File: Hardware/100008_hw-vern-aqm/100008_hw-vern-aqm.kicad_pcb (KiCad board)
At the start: 6 copper layers, 0 parts

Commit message: schematic and pcb work
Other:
- board outline added: 98 x 56.3 mm

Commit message: schematic and pcb layout
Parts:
- added C1: 1u, Capacitor_SMD:C_0805_2012Metric, F.Cu at (184.0, 324.5)
- added C10: 10u, Capacitor_SMD:C_0805_2012Metric, F.Cu at (108.9, 301.9)
- added C11: 10u, Capacitor_SMD:C_0805_2012Metric, F.Cu at (108.9, 303.9)
- added C12: 100n, Capacitor_SMD:C_0603_1608Metric, F.Cu at (221.2, 407.9)
- added C13: 100n, Capacitor_SMD:C_0603_1608Metric, F.Cu at (165.5, 313.0)
- added C14: 10u, Capacitor_SMD:C_0805_2012Metric, F.Cu at (162.1, 319.4)
- added C15: 100n, Capacitor_SMD:C_0603_1608Metric, F.Cu at (165.5, 316.2)
- added C16: 100n, Capacitor_SMD:C_0603_1608Metric, F.Cu at (146.4, 339.7)
- added C17: 100n, Capacitor_SMD:C_0603_1608Metric, F.Cu at (125.9, 351.8)
- added C18: 100n, Capacitor_SMD:C_0603_1608Metric, F.Cu at (144.8, 339.7)
- added C19: 100n, Capacitor_SMD:C_0603_1608Metric, F.Cu at (111.6, 351.8)
- added C2: 10u, Capacitor_SMD:C_0805_2012Metric, F.Cu at (179.6, 310.8)
- added C3: 10u, Capacitor_SMD:C_0805_2012Metric, F.Cu at (183.1, 310.8)
- added C4: 100n, Capacitor_SMD:C_0603_1608Metric, F.Cu at (179.4, 308.7)
- added C5: 10u, Capacitor_SMD:C_0805_2012Metric, F.Cu at (177.9, 304.2)
- added C6: 10u, Capacitor_SMD:C_0805_2012Metric, F.Cu at (180.0, 304.2)
- added C7: 100n, Capacitor_SMD:C_0603_1608Metric, F.Cu at (351.9, 406.0)
- added C8: 100n, Capacitor_SMD:C_0603_1608Metric, F.Cu at (109.1, 307.2)
- added C9: 100n, Capacitor_SMD:C_0603_1608Metric, F.Cu at (351.9, 411.0)
- added D1: ESD5Z3V3, Diode_SMD:D_SOD-523, F.Cu at (182.2, 334.4)
- added D2: ESD321DYAR, Diode_SMD:D_SOD-523, F.Cu at (182.2, 336.8)
- added D3: ESD321DYAR, Diode_SMD:D_SOD-523, F.Cu at (182.2, 339.3)
- added D4: ESD321DYAR, Diode_SMD:D_SOD-523, F.Cu at (140.1, 306.4)
- added D5: ESD321DYAR, Diode_SMD:D_SOD-523, F.Cu at (143.1, 306.4)
- added D6: LED, LED_SMD:LED_0603_1608Metric, F.Cu at (180.8, 315.1)
- added D7: LED, LED_SMD:LED_0603_1608Metric, F.Cu at (184.5, 315.1)
- added D8: LED, LED_SMD:LED_0603_1608Metric, F.Cu at (158.8, 305.7)
- added D9: LED, LED_SMD:LED_0603_1608Metric, F.Cu at (161.8, 305.7)
- added F1: Polyfuse, Fuse:Fuse_1206_3216Metric, F.Cu at (184.0, 322.3)
- added J1: Conn_01x14_Socket, Connector_PinHeader_2.54mm:PinHeader_1x14_P2.54mm_Vertical, F.Cu at (102.0, 344.7)
- added J2: USB4220-03-1000-C, Mechanical:USB_C_Receptacle_GCT_USB4220-03-xxxx-C_Vertical, F.Cu at (191.0, 328.2)
- added J3: Conn_01x06_MountingPin, Connector_JST:JST_GH_BM06B-GHS-TBT_1x06-1MP_P1.25mm_Vertical, F.Cu at (229.8, 337.8)
- added J4: Conn_01x03_Pin, Connector_PinHeader_2.54mm:PinHeader_1x03_P2.54mm_Vertical, F.Cu at (140.3, 303.1)
- added J5: Conn_01x06_Socket, Connector_PinHeader_2.00mm:PinHeader_1x06_P2.00mm_Vertical, F.Cu at (223.1, 343.0)
- added J6: Conn_01x04_Socket, Connector_PinHeader_2.54mm:PinHeader_1x04_P2.54mm_Vertical, F.Cu at (196.0, 332.0)
- added J7: Conn_01x05_Pin, Connector_PinHeader_2.54mm:PinHeader_1x05_P2.54mm_Vertical, F.Cu at (269.2, 284.4)
- added Q1: BC817, Package_TO_SOT_SMD:SOT-23, F.Cu at (150.1, 312.4)
- added Q2: BC817, Package_TO_SOT_SMD:SOT-23, F.Cu at (150.1, 315.9)
- added R1: 0R0, Resistor_SMD:R_0603_1608Metric, F.Cu at (279.9, 277.5)
- added R10: 0R0, Resistor_SMD:R_0603_1608Metric, F.Cu at (235.8, 333.6)
- added R11: 10k, Resistor_SMD:R_0603_1608Metric, F.Cu at (283.9, 287.6)
- added R12: 10k, Resistor_SMD:R_0603_1608Metric, F.Cu at (122.0, 323.2)
- added R13: 10k, Resistor_SMD:R_0603_1608Metric, F.Cu at (123.5, 323.2)
- added R14: 0R0, Resistor_SMD:R_0603_1608Metric, F.Cu at (179.4, 306.9)
- added R15: 10k, Resistor_SMD:R_0603_1608Metric, F.Cu at (182.4, 315.1)
- added R16: 10k, Resistor_SMD:R_0603_1608Metric, F.Cu at (186.1, 315.1)
- added R17: 10k, Resistor_SMD:R_0603_1608Metric, F.Cu at (109.1, 308.7)
- added R18: 5k1, Resistor_SMD:R_0603_1608Metric, F.Cu at (165.5, 309.8)
- added R19: 10k, Resistor_SMD:R_0603_1608Metric, F.Cu at (165.5, 311.4)
- added R2: 0R0, Resistor_SMD:R_0603_1608Metric, F.Cu at (279.9, 280.0)
- added R20: 1k, Resistor_SMD:R_0603_1608Metric, F.Cu at (165.5, 314.6)
- added R21: 0R0, Resistor_SMD:R_0603_1608Metric, F.Cu at (160.7, 323.9)
- added R22: 0R0, Resistor_SMD:R_0603_1608Metric, F.Cu at (159.2, 323.9)
- added R23: 10k, Resistor_SMD:R_0603_1608Metric, F.Cu at (153.7, 316.4)
- added R24: 10k, Resistor_SMD:R_0603_1608Metric, F.Cu at (153.7, 311.8)
- added R25: 0R0, Resistor_SMD:R_0603_1608Metric, F.Cu at (153.7, 314.9)
- added R26: 0R0, Resistor_SMD:R_0603_1608Metric, F.Cu at (153.7, 313.4)
- added R27: 10k, Resistor_SMD:R_0603_1608Metric, F.Cu at (158.8, 308.8)
- added R28: 1k, Resistor_SMD:R_0603_1608Metric, F.Cu at (160.3, 308.8)
- added R29: 1k, Resistor_SMD:R_0603_1608Metric, F.Cu at (161.8, 308.8)
- added R3: 5k1, Resistor_SMD:R_0603_1608Metric, F.Cu at (184.7, 328.9)
- added R30: 0R0, Resistor_SMD:R_0603_1608Metric, F.Cu at (153.7, 310.3)
- added R31: 0R0, Resistor_SMD:R_0603_1608Metric, F.Cu at (153.7, 317.9)
- added R32: 10k, Resistor_SMD:R_0603_1608Metric, F.Cu at (134.6, 302.7)
- added R33: 10k, Resistor_SMD:R_0603_1608Metric, F.Cu at (134.6, 304.2)
- added R34: 10k, Resistor_SMD:R_0603_1608Metric, F.Cu at (143.2, 339.7)
- added R4: 5k1, Resistor_SMD:R_0603_1608Metric, F.Cu at (184.7, 327.4)
- added R5: 0R0, Resistor_SMD:R_0603_1608Metric, F.Cu at (177.4, 327.6)
- added R6: 0R0, Resistor_SMD:R_0603_1608Metric, F.Cu at (177.3, 325.8)
- added R7: 0R0, Resistor_SMD:R_0603_1608Metric, F.Cu at (236.0, 339.4)
- added R8: 100R, Resistor_SMD:R_0603_1608Metric, F.Cu at (141.6, 306.4)
- added R9: 100R, Resistor_SMD:R_0603_1608Metric, F.Cu at (144.6, 306.4)
- added SW1: SW_Push, Button_Switch_SMD:SW_Tactile_SPST_NO_Straight_CK_PTS636Sx25SMTRLFS, F.Cu at (343.6, 406.0)
- added SW2: SW_Push, Button_Switch_SMD:SW_Tactile_SPST_NO_Straight_CK_PTS636Sx25SMTRLFS, F.Cu at (343.6, 411.2)
- added TP1: TestPoint, TestPoint:TestPoint_Pad_D1.5mm, F.Cu at (297.4, 298.9)
- added TP2: TestPoint, TestPoint:TestPoint_Pad_D1.5mm, F.Cu at (297.4, 302.5)
- added U1: AMS1117-3.3, Package_TO_SOT_SMD:SOT-223-3_TabPin2, F.Cu at (185.6, 306.1)
- added U2: ESP32-S3-WROOM-1, PCM_Espressif:ESP32-S3-WROOM-1, F.Cu at (121.8, 309.8)
- added U3: CP2102N-Axx-xQFN24, Package_DFN_QFN:QFN-24-1EP_4x4mm_P0.5mm_EP2.6x2.6mm, F.Cu at (159.9, 314.4)
- added U4: SCD40-D-R2, Sensor:Sensirion_SCD4x-1EP_10.1x10.1mm_P1.25mm_EP4.8x4.8mm, F.Cu at (118.8, 349.8)
- added U5: DPS368, Components:LGA8S145X65P2X4_200X250X110-V, F.Cu at (145.3, 346.1)
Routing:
- net +3V3: track 0.00 -> 9.73 mm
- net GND: track 0.00 -> 8.05 mm, vias 0 -> 1
- net Net-(U5-SDO): track 0.00 -> 5.28 mm
- net unconnected-(U5-~{CSB}-Pad2): track 0.00 -> 4.05 mm
- net I2C_SDA: track 0.00 -> 4.05 mm
- net I2C_SCL: track 0.00 -> 4.05 mm

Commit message: schematic and pcb general layout
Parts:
- added H2: MountingHole, MountingHole:MountingHole_4.5mm, F.Cu at (195.0, 352.9)
- added H3: MountingHole, MountingHole:MountingHole_4.5mm, F.Cu at (195.0, 303.4)
- added H4: MountingHole, MountingHole:MountingHole_4.5mm, F.Cu at (103.0, 303.4)
- moved C9 249.0 mm to (118.6, 324.0)
- moved SW2 240.0 mm to (117.8, 329.7), turned to -90 degrees
- moved C7 239.3 mm to (127.2, 324.0), turned to 180 degrees
- moved SW1 228.8 mm to (127.8, 329.7), turned to -90 degrees
- moved R1 184.6 mm to (109.0, 347.3)
- moved R2 182.8 mm to (109.0, 344.7)
- moved R11 166.5 mm to (121.3, 323.2), turned to 90 degrees
- moved C12 150.9 mm to (110.2, 305.7), turned to 180 degrees
- moved J7 135.2 mm to (140.4, 325.5), turned to 180 degrees
- moved TP2 88.5 mm to (209.9, 315.8)
- moved TP1 85.3 mm to (213.8, 315.7)
- moved R10 62.8 mm to (173.2, 339.3)
- moved R7 60.9 mm to (175.5, 346.2), turned to 180 degrees
- moved J3 53.2 mm to (178.2, 350.6), turned to 180 degrees
- moved J5 39.9 mm to (183.2, 343.3), turned to -90 degrees
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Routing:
- net JTAG_TCK: track 0.00 -> 17.9 mm
- net JTAG_TDO: track 0.00 -> 16.4 mm
- net UART0_RX: track 0.00 -> 16.2 mm
- net JTAG_TDI: track 0.00 -> 15.4 mm
- net JTAG_TMS: track 0.00 -> 14.1 mm
- net UART0_TX: track 0.00 -> 12.4 mm
- net Net-(D1-K): track 0.00 -> 5.84 mm
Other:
- outline, holes or cut-outs redrawn
- board text added: "3V3"
- board text added: "BACKLIGHT"
- board text added: "CS"
- board text added: "DC/RS"
- board text added: "GND"
- board text added: "GPIO0"
- board text added: "MISO"
- board text added: "MOSI"
- board text added: "RESET"
- board text added: "RX"
- board text added: "SCK"
- board text added: "SCL"
- board text added: "SDA"
- board text added: "TCK"
- board text added: "TDI"
- board text added: "TDO"
- board text added: "TMS"
- board text added: "TX"
- board text added: "T_CLK"
- board text added: "T_CS"
- board text added: "T_DIN"
- board text added: "T_IRQ"
- board text added: "T_OUT"
- board text added: "VBUS"
- board text added: "VCC"

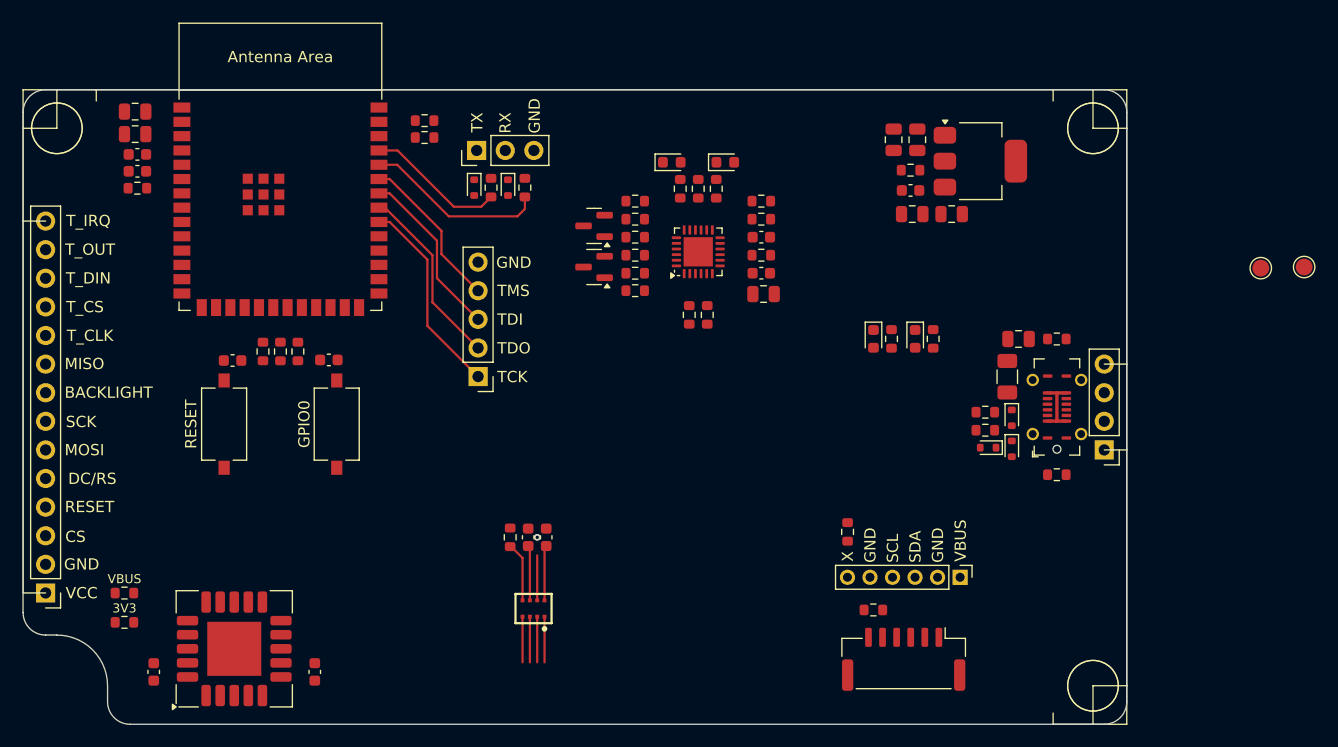
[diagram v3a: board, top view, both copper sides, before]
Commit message: schematic, pcb layout, added mouser shoping cart
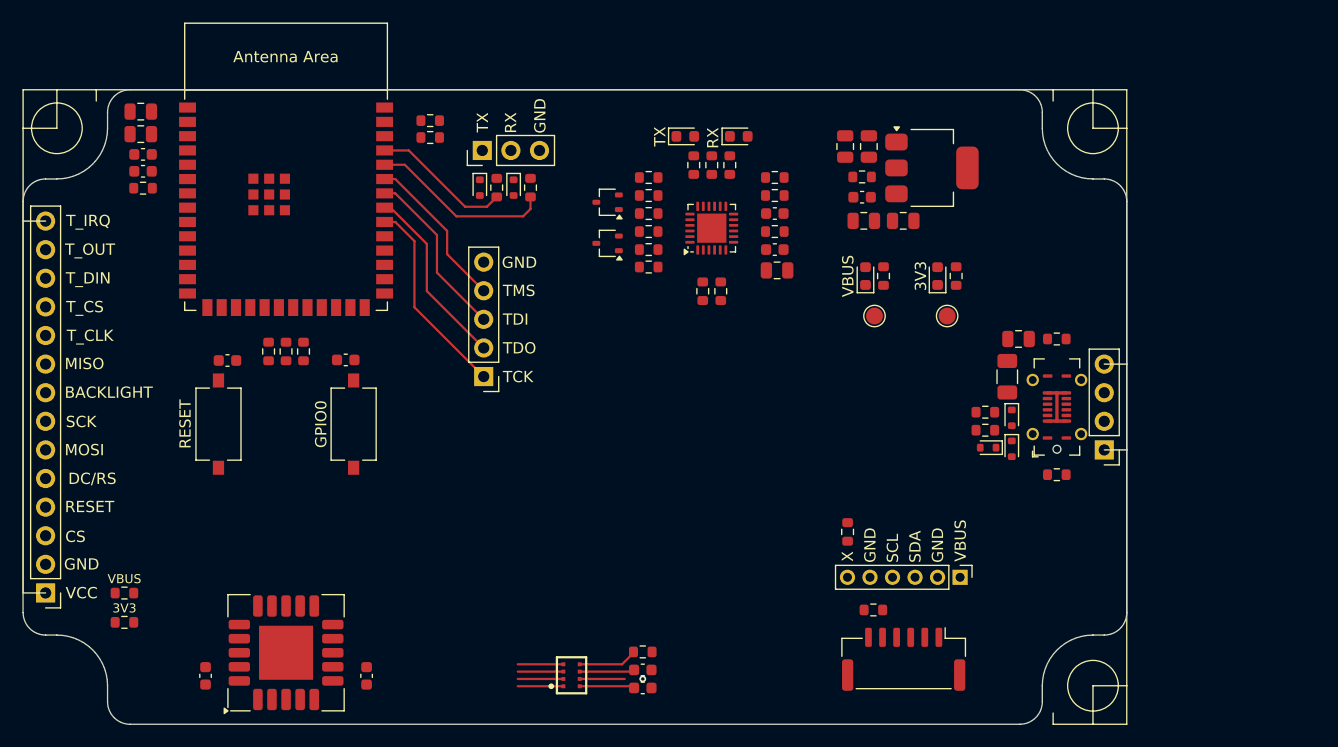
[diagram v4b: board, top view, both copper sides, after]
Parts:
- removed H2, H3, H4: MountingHole, MountingHole:MountingHole_4.5mm
- Q1, Q2: footprint Package_TO_SOT_SMD:SOT-23 -> Package_TO_SOT_SMD:SOT-323_SC-70
- moved TP1 38.4 mm to (175.6, 320.1)
- moved TP2 28.2 mm to (182.1, 320.1)
- moved C16 15.9 mm to (155.0, 353.1), turned to 0 degrees
- moved R34 15.6 mm to (155.0, 349.9), turned to 0 degrees
- moved C18 15.6 mm to (155.0, 351.5), turned to 0 degrees
- moved U5 6.82 mm to (148.7, 352.0), turned to 90 degrees
- moved R16 5.94 mm to (182.8, 316.5)
- moved D7 5.92 mm to (181.2, 316.5), turned to 90 degrees
- moved R15 5.62 mm to (176.4, 316.5)
- moved D6 5.62 mm to (174.8, 316.5), turned to 90 degrees
- moved C19 4.61 mm to (116.2, 352.0)
- moved C17 4.61 mm to (130.5, 352.0)
- moved U4 4.61 mm to (123.3, 350.0)
- moved C4 4.34 mm to (174.5, 309.5)
- moved C5 4.34 mm to (173.0, 305.0)
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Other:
- outline, holes or cut-outs redrawn

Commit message: pcb routing
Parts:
- added J8: Conn_01x04_MountingPin, Connector_JST:JST_SH_SM04B-SRSS-TB_1x04-1MP_P1.00mm_Horizontal, F.Cu at (184.5, 353.3)
- moved R10 14.5 mm to (160.3, 345.8), turned to -90 degrees
- moved R7 13.7 mm to (161.8, 345.8), turned to 90 degrees
- moved J5 9.52 mm to (174.0, 345.8)
- moved J3 9.38 mm to (169.0, 352.5)
- moved C16 3.69 mm to (151.3, 353.4)
- moved C18 3.69 mm to (151.3, 351.8)
- moved R34 3.69 mm to (151.3, 350.2)
- moved U5 3.69 mm to (145.0, 352.3)
- moved J7 1.71 mm to (140.8, 323.8)
- moved R11 1.55 mm to (121.8, 324.8)
- moved R12 1.55 mm to (123.3, 324.8)
- moved R13 1.55 mm to (124.9, 324.8)
- moved C4 0.92 mm to (175.4, 309.3)
- moved C5 0.92 mm to (173.9, 304.8)
- moved C6 0.92 mm to (176.0, 304.8)
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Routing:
- net USB_D-: track 0.00 -> 57.5 mm, vias 0 -> 2
- net USB_D+: track 0.00 -> 55.6 mm, vias 0 -> 2
- net +3V3: track 9.73 -> 50.7 mm
- net Net-(D3-K): track 0.00 -> 12.8 mm, vias 0 -> 2
- net Net-(D1-K): track 5.84 -> 17.2 mm, vias 0 -> 4
- net Net-(U3-VBUS): track 0.00 -> 9.57 mm
- net /Project Architecture/MCU - ESP32/GPIO0: track 0.00 -> 8.86 mm
- net Net-(D2-K): track 0.00 -> 8.18 mm
- net Net-(J2-CC2): track 0.00 -> 7.89 mm
- net Net-(J2-CC1): track 0.00 -> 7.78 mm, vias 0 -> 2
- net SD_CS(D3): track 0.00 -> 5.00 mm
- net SD_MOSI(CMD): track 0.00 -> 4.89 mm
- net SD_MISO(D0): track 0.00 -> 4.77 mm
- net Net-(D5-K): track 0.00 -> 4.27 mm
- net Net-(U3-~{SUSPEND}): track 0.00 -> 4.26 mm
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- added copper zone on F.Cu, net GND
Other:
- copper layers 6 -> 2
- board text added: "Air Quality Meter for VERN' University"
- board text added: "DPS368"
- board text added: "Designed by Šimunčić A."
- board text added: "SCD40"
- board text added: "SEN5x"
- board text added: "V1.0"
- board text added: "easyC"

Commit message: pcb layout
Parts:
- moved C11 1.67 mm to (109.5, 302.6), turned to 90 degrees
- moved C10 1.19 mm to (111.5, 302.6), turned to 90 degrees
- moved R17 0.78 mm to (110.5, 308.0)
- moved C8 0.75 mm to (110.5, 306.5)
- moved C12 0.73 mm to (110.5, 305.0)
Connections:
- U2 pad 10: SD_SCK(CLK) -> SPI_SCK
- U2 pad 11: unconnected-(U2-GPIO18/U1RXD/ADC2_CH7/CLK_OUT3-Pad11) -> LCD_BACKLIGHT
- U2 pad 12: SPI_SCK -> LCD_DC/RS
- U2 pad 18: LCD_DC/RS -> SPI_nCS_LCD
- U2 pad 19: LCD_BACKLIGHT -> SD_CS(D3)
- U2 pad 20: SD_CS(D3) -> SD_MOSI(CMD)
- U2 pad 21: SD_MOSI(CMD) -> SD_MISO(D0)
- U2 pad 22: SD_MISO(D0) -> SD_SCK(CLK)
- U2 pad 4: SPI_nCS_LCD -> unconnected-(U2-GPIO4/TOUCH4/ADC1_CH3-Pad4)
- U2 pad 5: SPI_nCS_TOUCH -> SPI_MISO
- U2 pad 6: SPI_MISO -> SPI_MOSI
- U2 pad 7: SPI_MOSI -> SPI_nCS_TOUCH
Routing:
- net +3V3: track 50.7 -> 235.9 mm, vias 0 -> 1
- net I2C_SCL: track 7.77 -> 40.5 mm, vias 0 -> 1
- net SPI_MOSI: track 0.00 -> 32.5 mm
- net SPI_nCS_LCD: track 0.00 -> 31.5 mm
- net I2C_SDA: track 7.77 -> 34.8 mm, vias 0 -> 1
- net /Project Architecture/MCU - ESP32/RESET: track 1.79 -> 27.7 mm, vias 0 -> 2
- net SPI_SCK: track 0.00 -> 24.9 mm
- net LCD_RESET: track 0.00 -> 24.7 mm
- net LCD_DC/RS: track 0.00 -> 24.4 mm
- net LCD_BACKLIGHT: track 0.00 -> 19.6 mm
- net SPI_nCS_TOUCH: track 0.00 -> 16.8 mm
- net SPI_MISO: track 0.00 -> 15.7 mm
- net GND: track 8.05 -> 18.4 mm, vias 1 -> 15
- net Net-(J1-Pin_1): track 0.00 -> 8.78 mm
- net Net-(J3-Pin_5): track 0.00 -> 7.83 mm
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
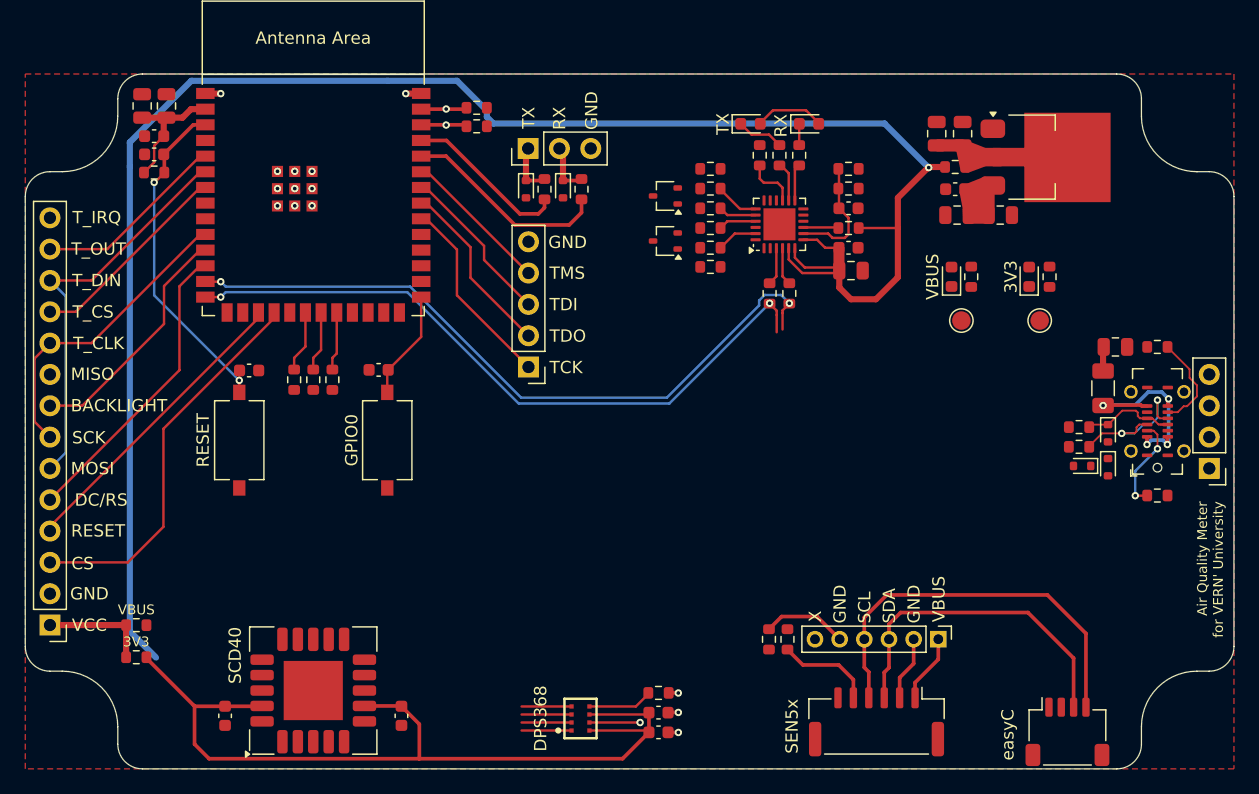
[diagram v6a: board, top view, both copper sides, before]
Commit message: PCB routing and DRC fixes
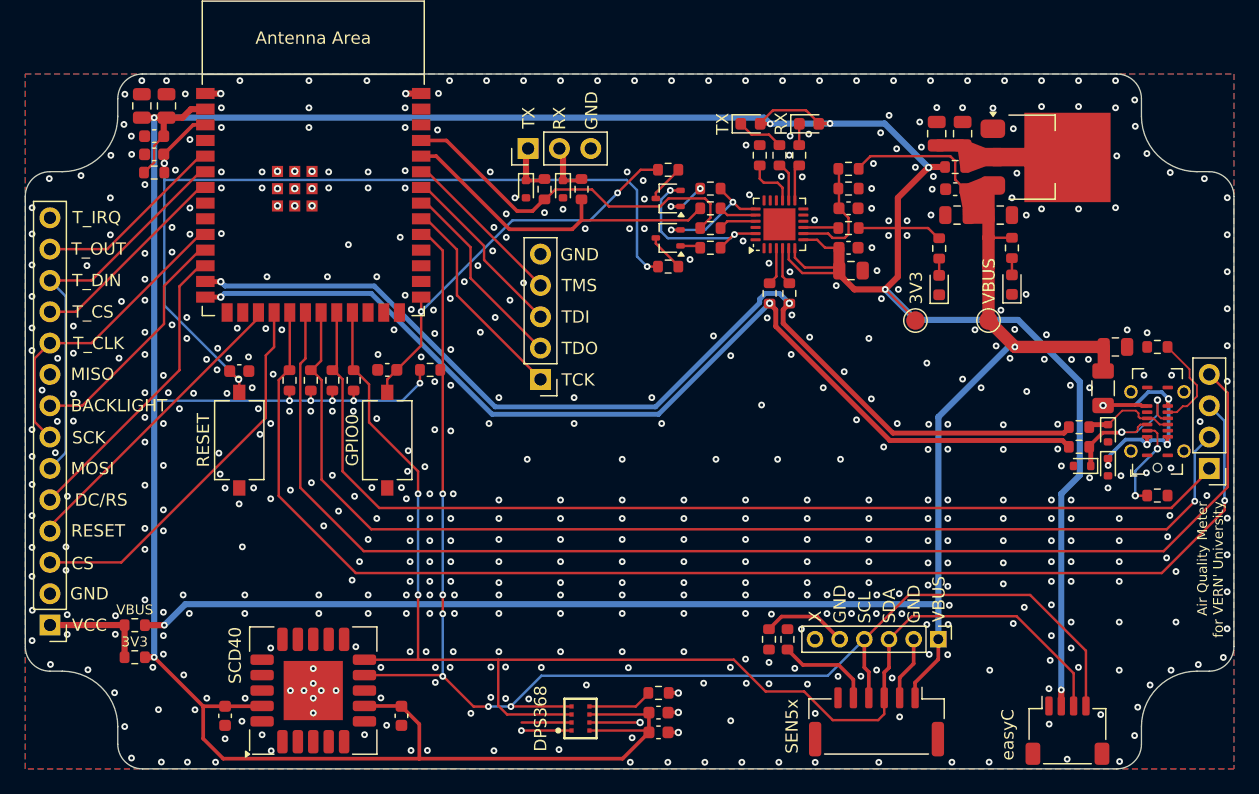
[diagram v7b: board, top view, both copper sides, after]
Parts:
- moved R32 24.2 mm to (126.6, 324.8), turned to 90 degrees
- moved R33 20.1 mm to (132.8, 324.0), turned to 0 degrees
- moved TP2 10.1 mm to (172.2, 320.0)
- moved R16 9.24 mm to (174.1, 314.1)
- moved R30 8.63 mm to (152.1, 315.6), turned to 0 degrees
- moved R31 8.59 mm to (152.1, 307.8), turned to 0 degrees
- moved D7 7.33 mm to (174.1, 317.1)
- moved D6 4.94 mm to (180.0, 317.1)
- moved R15 4.04 mm to (180.0, 314.1)
- moved R13 3.48 mm to (121.4, 324.8)
- moved Q2 3.46 mm to (152.1, 310.1)
- moved Q1 3.41 mm to (152.1, 313.3)
- moved R11 3.10 mm to (124.9, 324.8)
- moved TP1 2.20 mm to (178.1, 320.0)
- moved J7 1.40 mm to (141.8, 324.8)
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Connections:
- U2 pad 19: SD_CS(D3) -> SD_MISO(D0)
- U2 pad 20: SD_MOSI(CMD) -> SD_SCK(CLK)
- U2 pad 21: SD_MISO(D0) -> SD_MOSI(CMD)
- U2 pad 22: SD_SCK(CLK) -> SD_CS(D3)
- U2 pad 23: unconnected-(U2-GPIO21-Pad23) -> I2C_SDA
- U2 pad 31: unconnected-(U2-GPIO38/FSPIWP/SUBSPIWP-Pad31) -> I2C_SCL
- U2 pad 38: I2C_SCL -> unconnected-(U2-GPIO2/TOUCH2/ADC1_CH1-Pad38)
- U2 pad 39: I2C_SDA -> unconnected-(U2-GPIO1/TOUCH1/ADC1_CH0-Pad39)
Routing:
- net VBUS: track 7.50 -> 131.0 mm, vias 0 -> 2
- net SD_SCK(CLK): track 0.00 -> 103.6 mm
- net SD_MISO(D0): track 4.77 -> 105.7 mm, vias 0 -> 1
- net SD_MOSI(CMD): track 4.89 -> 93.4 mm, vias 0 -> 1
- net SD_CS(D3): track 5.00 -> 86.3 mm
- net I2C_SDA: track 34.8 -> 111.5 mm, vias 1 -> 2
- net I2C_SCL: track 40.5 -> 116.3 mm, vias 1 -> 6
- net +3V3: track 235.9 -> 310.4 mm, vias 1 -> 12
- net /Project Architecture/MCU - ESP32/RESET: track 27.7 -> 74.8 mm, vias 2 -> 3
- net USB_D+: track 55.6 -> 84.1 mm
- net USB_D-: track 57.5 -> 85.4 mm
- net /Project Architecture/MCU - ESP32/GPIO0: track 8.86 -> 32.8 mm, vias 0 -> 2
- net UART0_TX: track 13.3 -> 29.9 mm
- net UART0_RX: track 16.8 -> 27.9 mm
- net /Project Architecture/MCU - ESP32/UART0_nDTR: track 3.31 -> 14.1 mm, vias 0 -> 2
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- added copper zone on B.Cu, net GND
